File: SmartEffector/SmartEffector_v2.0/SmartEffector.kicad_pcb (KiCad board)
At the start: 2 copper layers, 83.2 x 72.1 mm, 57 parts, among them M1 FID, M10 M_2.9mm, M11 M_2.9mm, M13 Ziptie, M16 12mm, M2 FID, M3 M_2.9mm, M4 M_2.9mm, M5 M_2.9mm, M6 M_2.9mm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

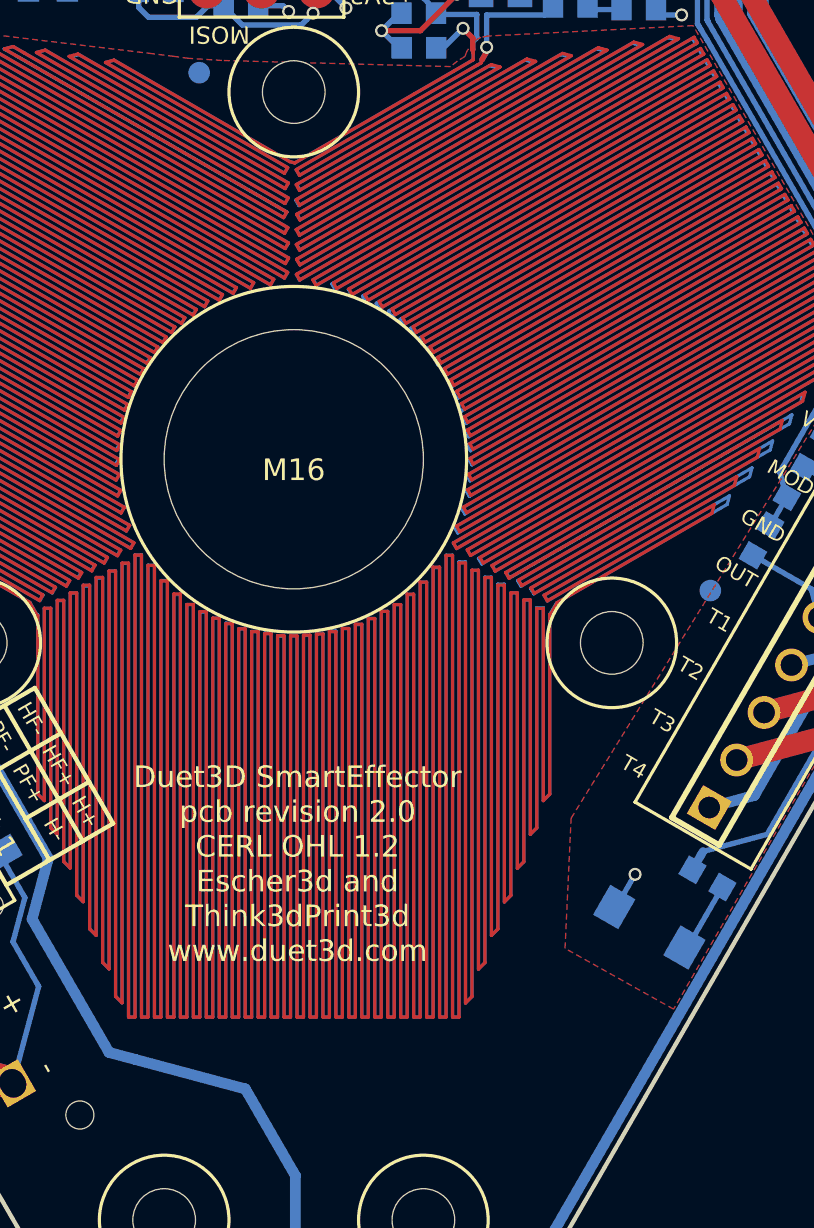
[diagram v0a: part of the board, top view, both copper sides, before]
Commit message: Updated some schematic issues
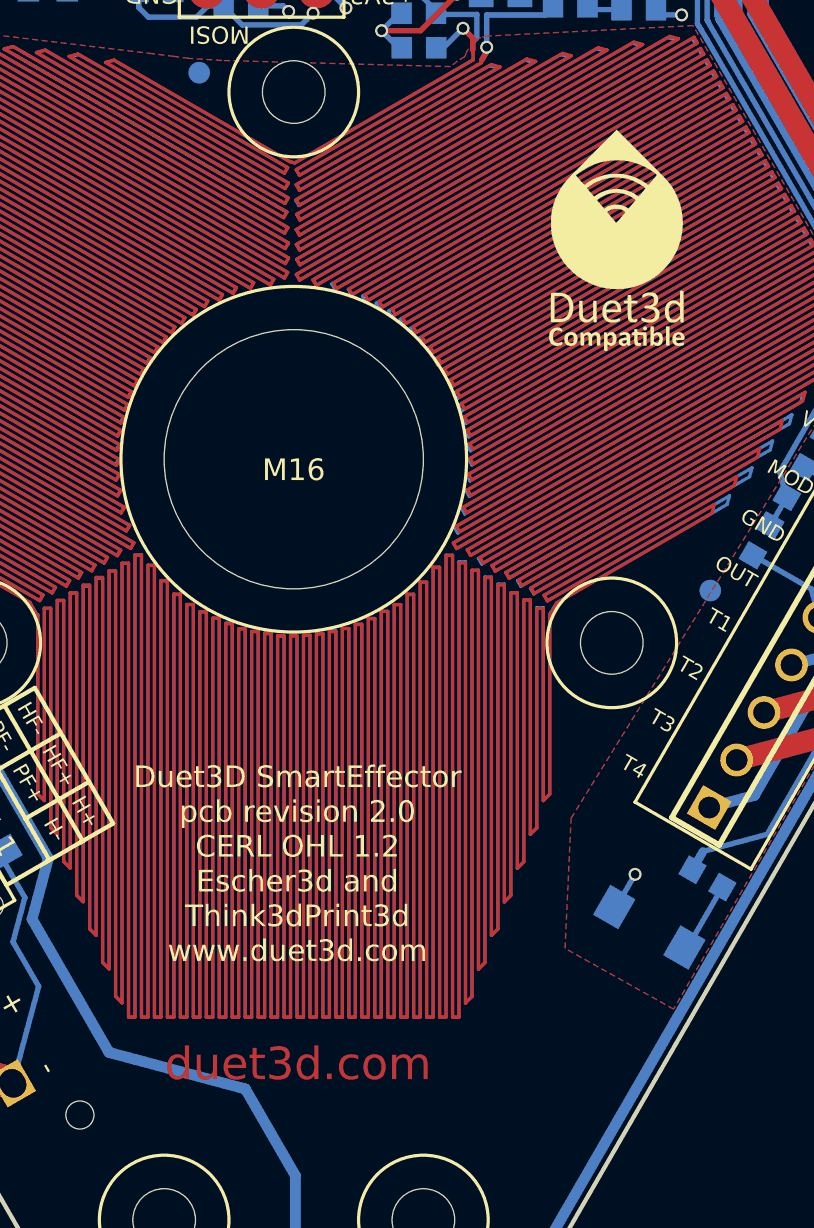
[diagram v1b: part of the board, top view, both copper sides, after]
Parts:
- added M15: Duet3D Logo, complib:LOGO_Duet3dCompatible, F.Cu at (-46.9, -132.9)
- C6: value 22u<20% -> 22u
- U2: value ATtiny44A-MMH-PAD -> ATtiny44A-MUR
